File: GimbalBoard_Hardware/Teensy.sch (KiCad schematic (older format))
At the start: 1 part, among them U1 Teensy4.1_DEV-16771

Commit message: added more text
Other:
- note added: "Teensy"
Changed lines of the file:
@@
 $Descr A4 11693 8268
 encoding utf-8
-Sheet 7 8
+Sheet 6 8
 Title ""
 Date ""
@@
 Text HLabel 4550 5700 2    50   Input ~ 0
 GND
+Text Notes 3550 1450 0    79   ~ 0
+Teensy
 $EndSCHEMATC

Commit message: added labels, numbered everything, added no connection to pins. Still can't get past a couple pf errors in the electrical rules check
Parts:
- renumbered U1 to U5
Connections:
- no-connect marks 0 -> 35
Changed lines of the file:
@@
 P 3750 3900
 AR Path="/61642BE3" Ref="U?"  Part="1"
-AR Path="/6163DAA7/61642BE3" Ref="U1"  Part="1"
-F 0 "U1" H 3750 6067 50  0000 C CNN
+AR Path="/6163DAA7/61642BE3" Ref="U5"  Part="1"
+F 0 "U5" H 3750 6067 50  0000 C CNN
 F 1 "Teensy4.1_DEV-16771" H 3750 5976 50  0000 C CNN
 F 2 "MODULE_DEV-16771" H 5850 3600 50  0001 L BNN
@@
 Text Notes 3550 1450 0    79   ~ 0
 Teensy
+NoConn ~ 2950 2500
+NoConn ~ 2950 2800
+NoConn ~ 2950 2900
+NoConn ~ 2950 3100
+NoConn ~ 2950 3700
+NoConn ~ 2950 3800
+NoConn ~ 2950 4400
+NoConn ~ 2950 4500
+NoConn ~ 2950 4700
+NoConn ~ 2950 4800
+NoConn ~ 2950 4900
+NoConn ~ 2950 5000
+NoConn ~ 2950 5100
+NoConn ~ 2950 5200
+NoConn ~ 2950 5300
+NoConn ~ 2950 5400
+NoConn ~ 2950 5500
+NoConn ~ 4550 5500
+NoConn ~ 4550 5000
+NoConn ~ 4550 4900
+NoConn ~ 4550 4800
+NoConn ~ 4550 4700
+NoConn ~ 4550 4000
+NoConn ~ 4550 3900
+NoConn ~ 4550 3700
+NoConn ~ 4550 3600
+NoConn ~ 4550 3200
+NoConn ~ 4550 3100
+NoConn ~ 4550 2900
+NoConn ~ 4550 2800
+NoConn ~ 4550 2700
+NoConn ~ 4550 2600
+NoConn ~ 4550 2500
+NoConn ~ 4550 2300
+NoConn ~ 4550 2200
 $EndSCHEMATC

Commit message: sheet has been reviewed
schematic has been reviewed. and resister values have been changed. as well as a ground being added
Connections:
- net GND: now also U5.USB_GND1 (USB_GND), U5.USB_GND2 (USB_GND)
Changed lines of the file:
@@
 Text HLabel 4550 4300 2    50   Input ~ 0
 Servo_Manual_Control_Left
-Text HLabel 4550 5700 2    50   Input ~ 0
-GND
 Text Notes 3550 1450 0    79   ~ 0
 Teensy
@@
 NoConn ~ 4550 2300
 NoConn ~ 4550 2200
+Text HLabel 4550 5800 2    50   Input ~ 0
+GND
+Text HLabel 4550 5700 2    50   Input ~ 0
+GND
 $EndSCHEMATC

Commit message: Post PDR changes
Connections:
- net Servo_Digital_Control: no longer names the net of U5.10 (CS1)
- no-connect marks 35 -> 37
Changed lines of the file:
@@
 $Descr A4 11693 8268
 encoding utf-8
-Sheet 6 8
+Sheet 4 5
 Title ""
 Date ""
@@
 Text HLabel 4550 2000 2    50   Input ~ 0
 +5VL
-Text HLabel 4550 4100 2    50   Input ~ 0
-Servo_Digital_Control
 Text HLabel 4550 4400 2    50   Input ~ 0
 Servo_Manual_Control_Right
@@
 Text HLabel 4550 5700 2    50   Input ~ 0
 GND
+NoConn ~ 4550 4100
+NoConn ~ 4550 2100
 $EndSCHEMATC

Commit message: now powering the teensy w 3.3VL instead of 5VL
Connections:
- net +3.3VL: now reaches U5.3.3V_1 (3.3V), U5.3.3V_2 (3.3V), U5.3.3V_3 (3.3V)
- net +5VL: no longer names the net of U5.5V
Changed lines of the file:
@@
 $Descr A4 11693 8268
 encoding utf-8
-Sheet 4 5
+Sheet 3 5
 Title ""
 Date ""
@@
 	1    0    0    -1
 $EndComp
-Text HLabel 4550 2000 2    50   Input ~ 0
-+5VL
 Text HLabel 4550 4400 2    50   Input ~ 0
 Servo_Manual_Control_Right
@@
 GND
 NoConn ~ 4550 4100
-NoConn ~ 4550 2100
+Text HLabel 4550 2100 2    50   Input ~ 0
++3.3VL
+NoConn ~ 4550 2000
 $EndSCHEMATC

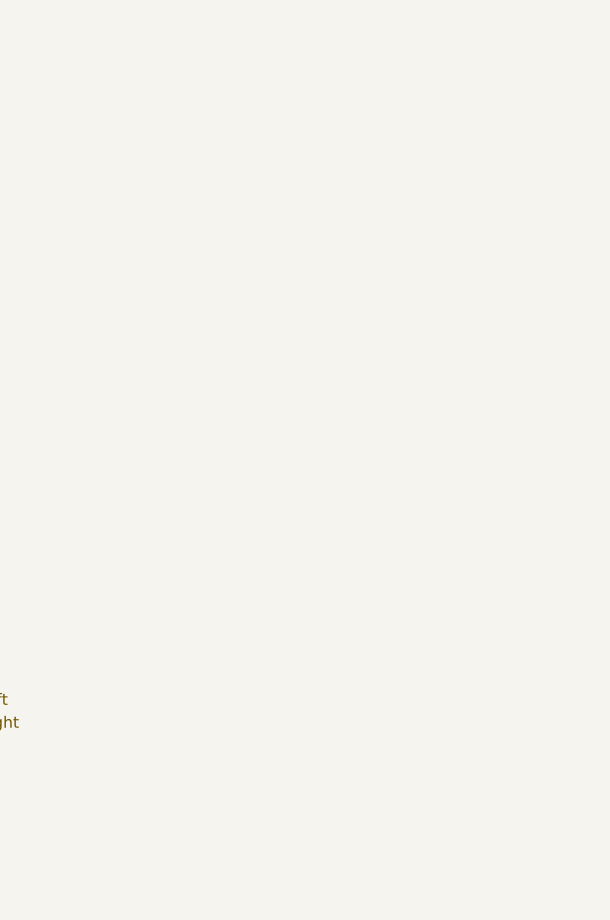
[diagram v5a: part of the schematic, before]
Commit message: Footprints finished
the footprints are finished. the RJ45 connector has been added for eithernet.
the net is in the layout thing but I haven't moved anything yet
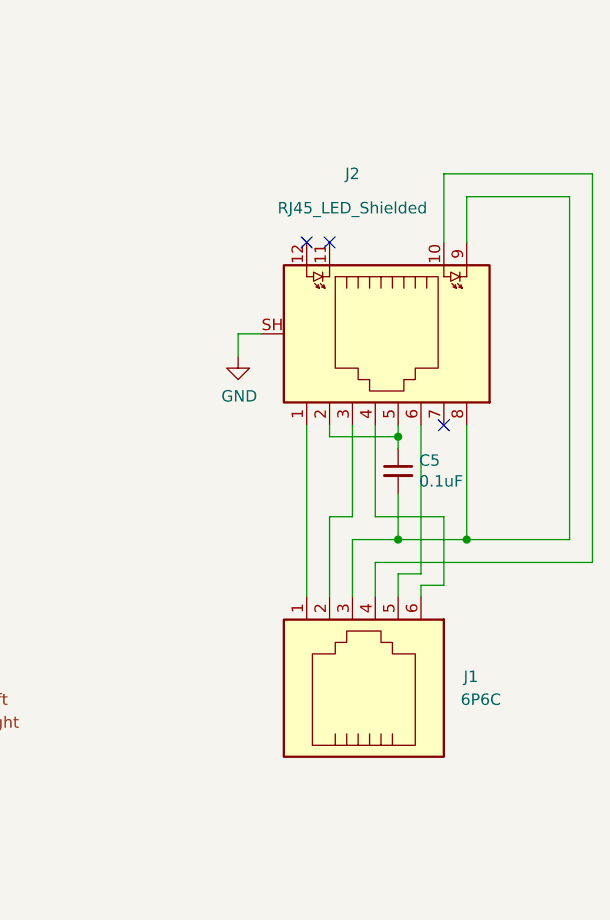
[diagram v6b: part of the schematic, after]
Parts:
- added C5: 0.1uF, Capacitor_SMD:C_0201_0603Metric_Pad0.64x0.40mm_HandSolder, symbol Device:C_Small
- added J1: 6P6C, Connector_PinHeader_2.00mm:PinHeader_2x03_P2.00mm_Vertical, symbol Connector:6P6C
- added J2: RJ45_LED_Shielded, MRDT_Connectors:RJ45_Teensy, symbol Connector:RJ45_LED_Shielded
- U5: footprint MODULE_DEV-16771 -> MRDT_Shields:Teensy_4_1_Vertical
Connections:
- net GND: now also J2.SH
- new net: J1.1, J2.1
- new net: J1.4, J2.10
- new net: C5.1, J2.2, J2.5
- new net: J1.2, J2.3
- new net: J1.6, J2.4
- new net: J1.5, J2.6
- new net: C5.2, J1.3, J2.8, J2.9
- no-connect marks 37 -> 40
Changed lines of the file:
@@
 F 0 "U5" H 3750 6067 50  0000 C CNN
 F 1 "Teensy4.1_DEV-16771" H 3750 5976 50  0000 C CNN
-F 2 "MODULE_DEV-16771" H 5850 3600 50  0001 L BNN
+F 2 "MRDT_Shields:Teensy_4_1_Vertical" H 5850 3600 50  0001 L BNN
 F 3 "" H 3750 3900 50  0001 L BNN
 F 4 "Manufacturer recommendations" H 5850 3350 50  0001 L BNN "STANDARD"
@@
 +3.3VL
 NoConn ~ 4550 2000
+$Comp
+L Connector:RJ45_LED_Shielded J2
+U 1 1 6191223A
+P 7150 2700
+F 0 "J2" V 6450 2600 50  0000 C CNN
+F 1 "RJ45_LED_Shielded" V 6600 2600 50  0000 C CNN
+F 2 "MRDT_Connectors:RJ45_Teensy" V 7150 2725 50  0001 C CNN
+F 3 "~" V 7150 2725 50  0001 C CNN
+	1    7150 2700
+	0    1    1    0
+$EndComp
+NoConn ~ 6850 2300
+NoConn ~ 6950 2300
+Wire Wire Line
+	6850 3100 6850 3850
+Wire Wire Line
+	7050 3100 7050 3500
+Wire Wire Line
+	7050 3500 6950 3500
+Wire Wire Line
+	6950 3500 6950 3850
+$Comp
+L Device:C_Small C5
+U 1 1 6191F909
+P 7250 3300
+F 0 "C5" H 7342 3346 50  0000 L CNN
+F 1 "0.1uF" H 7342 3255 50  0000 L CNN
+F 2 "Capacitor_SMD:C_0201_0603Metric_Pad0.64x0.40mm_HandSolder" H 7250 3300 50  0001 C CNN
+F 3 "~" H 7250 3300 50  0001 C CNN
+	1    7250 3300
+	1    0    0    -1
+$EndComp
+Wire Wire Line
+	7250 3100 7250 3150
+Wire Wire Line
+	7250 3400 7250 3600
+Wire Wire Line
+	7250 3600 7050 3600
+Wire Wire Line
+	7050 3600 7050 3850
+Wire Wire Line
+	7250 3600 7550 3600
+Wire Wire Line
+	7550 3600 7550 3100
+Connection ~ 7250 3600
+Wire Wire Line
+	7550 2300 7550 2100
+Wire Wire Line
+	7550 2100 8000 2100
+Wire Wire Line
+	8000 2100 8000 3600
+Wire Wire Line
+	8000 3600 7550 3600
+Connection ~ 7550 3600
+Wire Wire Line
+	7450 2300 7450 2000
+Wire Wire Line
+	7450 2000 8100 2000
+Wire Wire Line
+	8100 2000 8100 3700
+Wire Wire Line
+	7150 3700 7150 3850
+$Comp
+L Connector:6P6C J1
+U 1 1 6191A7E8
+P 7050 4250
+F 0 "J1" V 7100 4800 50  0000 R CNN
+F 1 "6P6C" V 7000 4900 50  0000 R CNN
+F 2 "Connector_PinHeader_2.00mm:PinHeader_2x03_P2.00mm_Vertical" V 7050 4275 50  0001 C CNN
+F 3 "~" V 7050 4275 50  0001 C CNN
+	1    7050 4250
+	0    1    -1   0
+$EndComp
+Wire Wire Line
+	7150 3700 8100 3700
+Wire Wire Line
+	6950 3100 6950 3150
+Wire Wire Line
+	6950 3150 7250 3150
+Connection ~ 7250 3150
+Wire Wire Line
+	7250 3150 7250 3200
+NoConn ~ 7450 3100
+Wire Wire Line
+	7350 3100 7350 3750
+Wire Wire Line
+	7350 3750 7250 3750
+Wire Wire Line
+	7250 3750 7250 3850
+Wire Wire Line
+	7150 3100 7150 3500
+Wire Wire Line
+	7150 3500 7450 3500
+Wire Wire Line
+	7450 3500 7450 3800
+Wire Wire Line
+	7450 3800 7350 3800
+Wire Wire Line
+	7350 3800 7350 3850
+$Comp
+L power:GND #PWR01
+U 1 1 61925256
+P 6550 2800
+F 0 "#PWR01" H 6550 2550 50  0001 C CNN
+F 1 "GND" H 6555 2627 50  0000 C CNN
+F 2 "" H 6550 2800 50  0001 C CNN
+F 3 "" H 6550 2800 50  0001 C CNN
+	1    6550 2800
+	1    0    0    -1
+$EndComp
+Wire Wire Line
+	6550 2800 6550 2700
+Wire Wire Line
+	6550 2700 6650 2700
 $EndSCHEMATC

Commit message: moved footprints
I moved some footprints around and asked some questions about trace width. as well as fixed the ethernet cap footprint
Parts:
- C5: footprint Capacitor_SMD:C_0201_0603Metric_Pad0.64x0.40mm_HandSolder -> Capacitor_SMD:C_0603_1608Metric_Pad1.08x0.95mm_HandSolder
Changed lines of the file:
@@
 F 0 "C5" H 7342 3346 50  0000 L CNN
 F 1 "0.1uF" H 7342 3255 50  0000 L CNN
-F 2 "Capacitor_SMD:C_0201_0603Metric_Pad0.64x0.40mm_HandSolder" H 7250 3300 50  0001 C CNN
+F 2 "Capacitor_SMD:C_0603_1608Metric_Pad1.08x0.95mm_HandSolder" H 7250 3300 50  0001 C CNN
 F 3 "~" H 7250 3300 50  0001 C CNN
 	1    7250 3300
